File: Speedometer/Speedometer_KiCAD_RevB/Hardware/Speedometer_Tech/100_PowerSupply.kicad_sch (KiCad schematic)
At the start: 38 parts, among them U1000 TPS51385, U1020 TPS51385

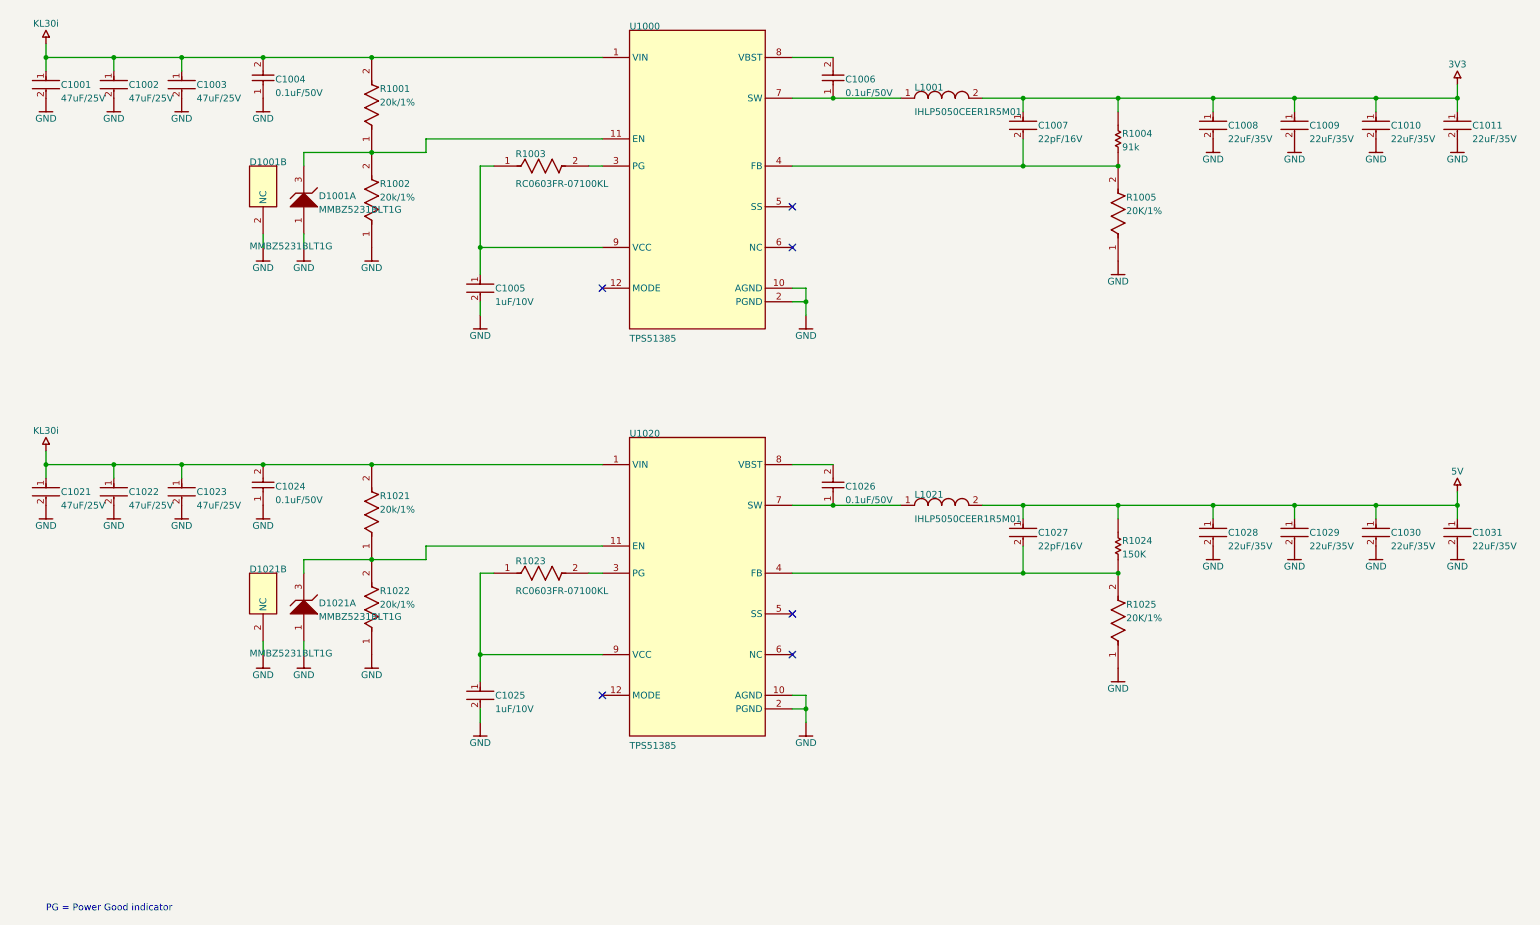
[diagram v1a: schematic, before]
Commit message: Speedometer DRC mostly passed
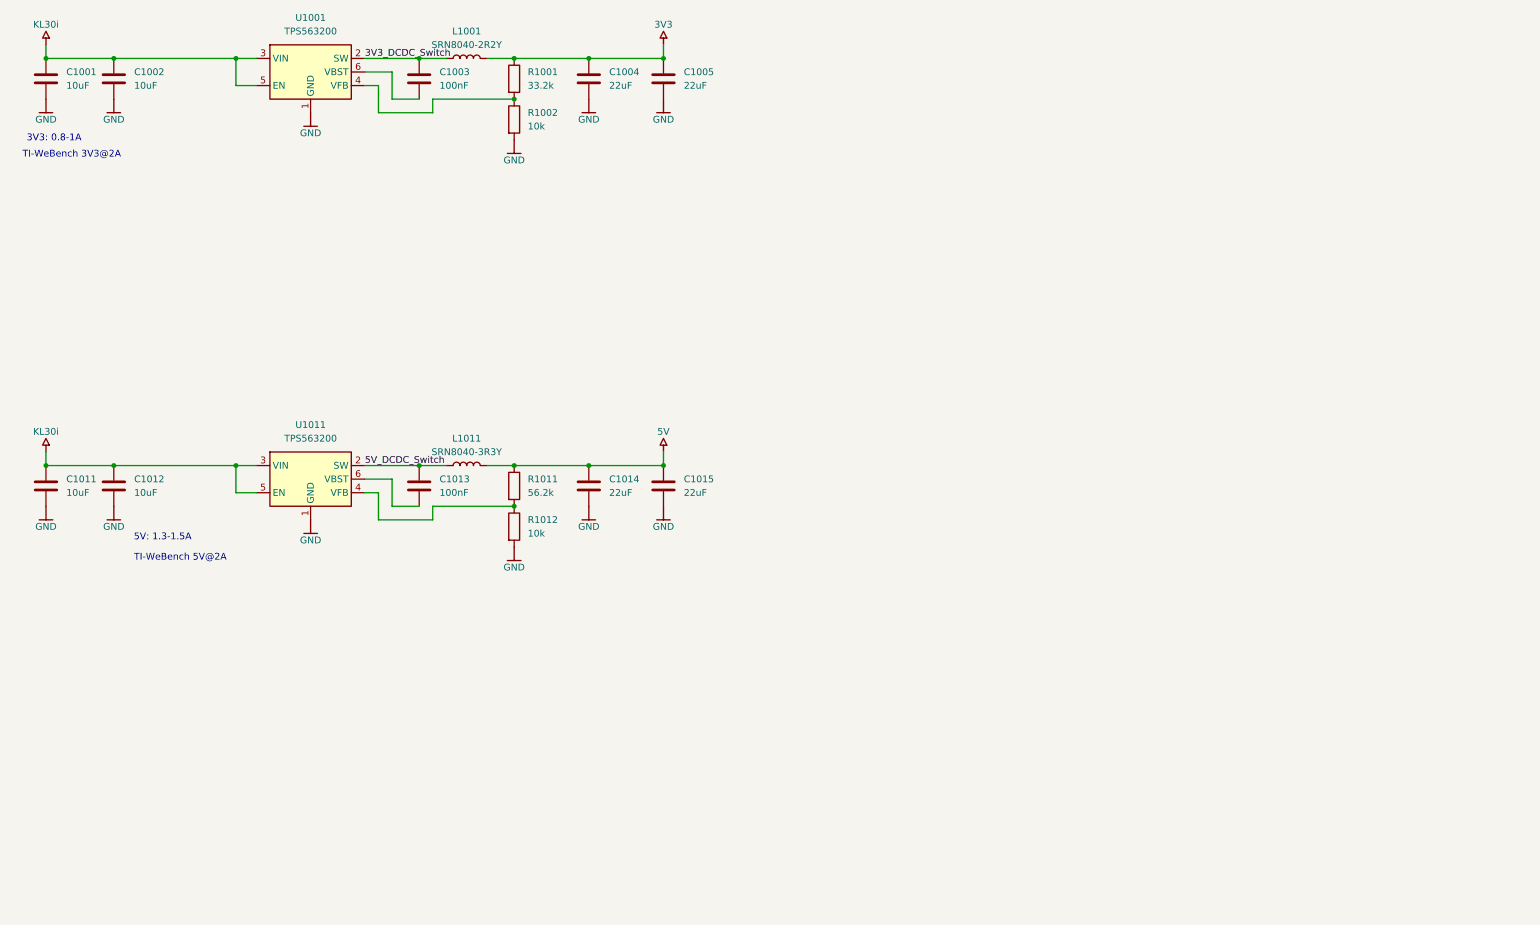
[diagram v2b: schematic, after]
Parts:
- removed C1001, C1002, C1003, C1021, C1022, C1023: 47uF/25V, FP-C3216-160-0_2-MFG, symbol Speedometer_Tech-altium-import:Designator_0_11868f565c42a9108669ba33697ecf6
- removed C1004, C1006, C1024, C1026: 0.1uF/50V, CAPC2013X135X45ML10T25, symbol Speedometer_Tech-altium-import:Designator_1_CAP-NP-2
- removed C1005, C1025: 1uF/10V, FP-C0603-CG-MFG, symbol Speedometer_Tech-altium-import:Designator_0_02cd4be3c70576c341d710602a673aa
- removed C1007, C1027: 22pF/16V, FP-C0603C-CF-MFG, symbol Speedometer_Tech-altium-import:Designator_0_b4654b650e69147ec39a6b967a45e02
- removed C1008, C1009, C1010, C1011, C1028, C1029, C1030, C1031: 22uF/35V, FP-C3216-160-0_2-IPC_B, symbol Speedometer_Tech-altium-import:Designator_0_11868f565c42a9108669ba33697ecf6
- removed D1001, D1021: MMBZ5231BLT1G, ONSC-SOT-23-3-318-08_V, symbol Speedometer_Tech-altium-import:Designator_3_ONSC-A1K3-3
- removed L1001, L1021: IHLP5050CEER1R5M01, IHLP5050CEER1R5M01, symbol Speedometer_Tech-altium-import:Designator_0_IHLP5050CEER1R5M01
- removed R1001, R1002, R1021, R1022: 20k/1%, FP-RC0603-0_55-IPC_C, symbol Speedometer_Tech-altium-import:Designator_1_1029c3af85768c4190bb7ad29bc67b5
- removed R1003, R1023: RC0603FR-07100KL, FP-RC0603-0_55-MFG, symbol Speedometer_Tech-altium-import:Designator_0_1029c3af85768c4190bb7ad29bc67b5
- removed R1004: 91k, RESC1609X50X30NL10T20, symbol Speedometer_Tech-altium-import:Designator_1_RES_0
- removed R1005, R1025: 20K/1%, FP-RC0603-0_55-IPC_C, symbol Speedometer_Tech-altium-import:Designator_1_1029c3af85768c4190bb7ad29bc67b5
- removed R1024: 150K, RESC1608X55X30NL15T15, symbol Speedometer_Tech-altium-import:Designator_1_RES_0
- removed U1000, U1020: TPS51385, TPS51386, symbol Speedometer_Tech-altium-import:Designator_0_TPS51386
- added C1001, C1002, C1011, C1012: 10uF, Capacitor_SMD:C_0805_2012Metric, symbol Device:C
- added C1003, C1013: 100nF, Capacitor_SMD:C_0805_2012Metric, symbol Device:C
- added C1004, C1005, C1014, C1015: 22uF, Capacitor_SMD:C_0805_2012Metric, symbol Device:C
- added L1001: SRN8040-2R2Y, Inductor_SMD:L_Bourns-SRN8040_8x8.15mm, symbol Device:L
- added L1011: SRN8040-3R3Y, Inductor_SMD:L_Bourns-SRN8040_8x8.15mm, symbol Device:L
- added R1001: 33.2k, Resistor_SMD:R_0603_1608Metric, symbol Device:R
- added R1002, R1012: 10k, Resistor_SMD:R_0603_1608Metric, symbol Device:R
- added R1011: 56.2k, Resistor_SMD:R_0603_1608Metric, symbol Device:R
- added U1001, U1011: TPS563200, Package_TO_SOT_SMD:SOT-23-6, symbol Regulator_Switching:TPS563200
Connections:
- net 3V3: now also C1004.1, C1005.1, L1001.2, R1001.1
- net 5V: now also C1014.1, C1015.1, L1011.2, R1011.1
- net GND: now also C1001.2, C1002.2, C1004.2, C1005.2, C1011.2, C1012.2, C1014.2, C1015.2, R1002.2, R1012.2, U1001.1 (GND), U1011.1 (GND)
- net KL30i: now also C1001.1, C1002.1, C1011.1, C1012.1, U1001.3 (VIN), U1001.5 (EN), U1011.3 (VIN), U1011.5 (EN)
- new net: R1001.2, R1002.1, U1001.4 (VFB)
- new net: C1013.2, U1011.6 (VBST)
- new net: R1011.2, R1012.1, U1011.4 (VFB)
- new net: C1003.2, U1001.6 (VBST)
- new net 3V3_DCDC_Switch: C1003.1, L1001.1, U1001.2 (SW)
- new net 5V_DCDC_Switch: C1013.1, L1011.1, U1011.2 (SW)
- no-connect marks 6 -> 0
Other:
- note added: "3V3: 0.8-1A"
- note added: "5V: 1.3-1.5A"
- note added: "TI-WeBench 3V3@2A"
- note added: "TI-WeBench 5V@2A"
- note removed: "PG = Power Good indicator"

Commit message: pcb should be done now
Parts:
- added C1006, C1016: 22uF, Capacitor_SMD:C_0805_2012Metric, symbol Device:C
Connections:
- net 3V3: now also C1006.1
- net 5V: now also C1016.1
- net GND: now also C1006.2, C1016.2
